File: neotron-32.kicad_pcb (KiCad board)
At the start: 2 copper layers, 166.9 x 140.7 mm, 93 parts, among them J1 Conn_02x06, J10 micro SD Card, J11 Conn_02x13_Top_Bottom, J12 AVR-ISP-6, J13 DE9 Male, J14 DE9 Male, J15 Double-mini-DIN-6, J17 DB15HD_Female, J18 Conn_02x05, J2 Conn_02x06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

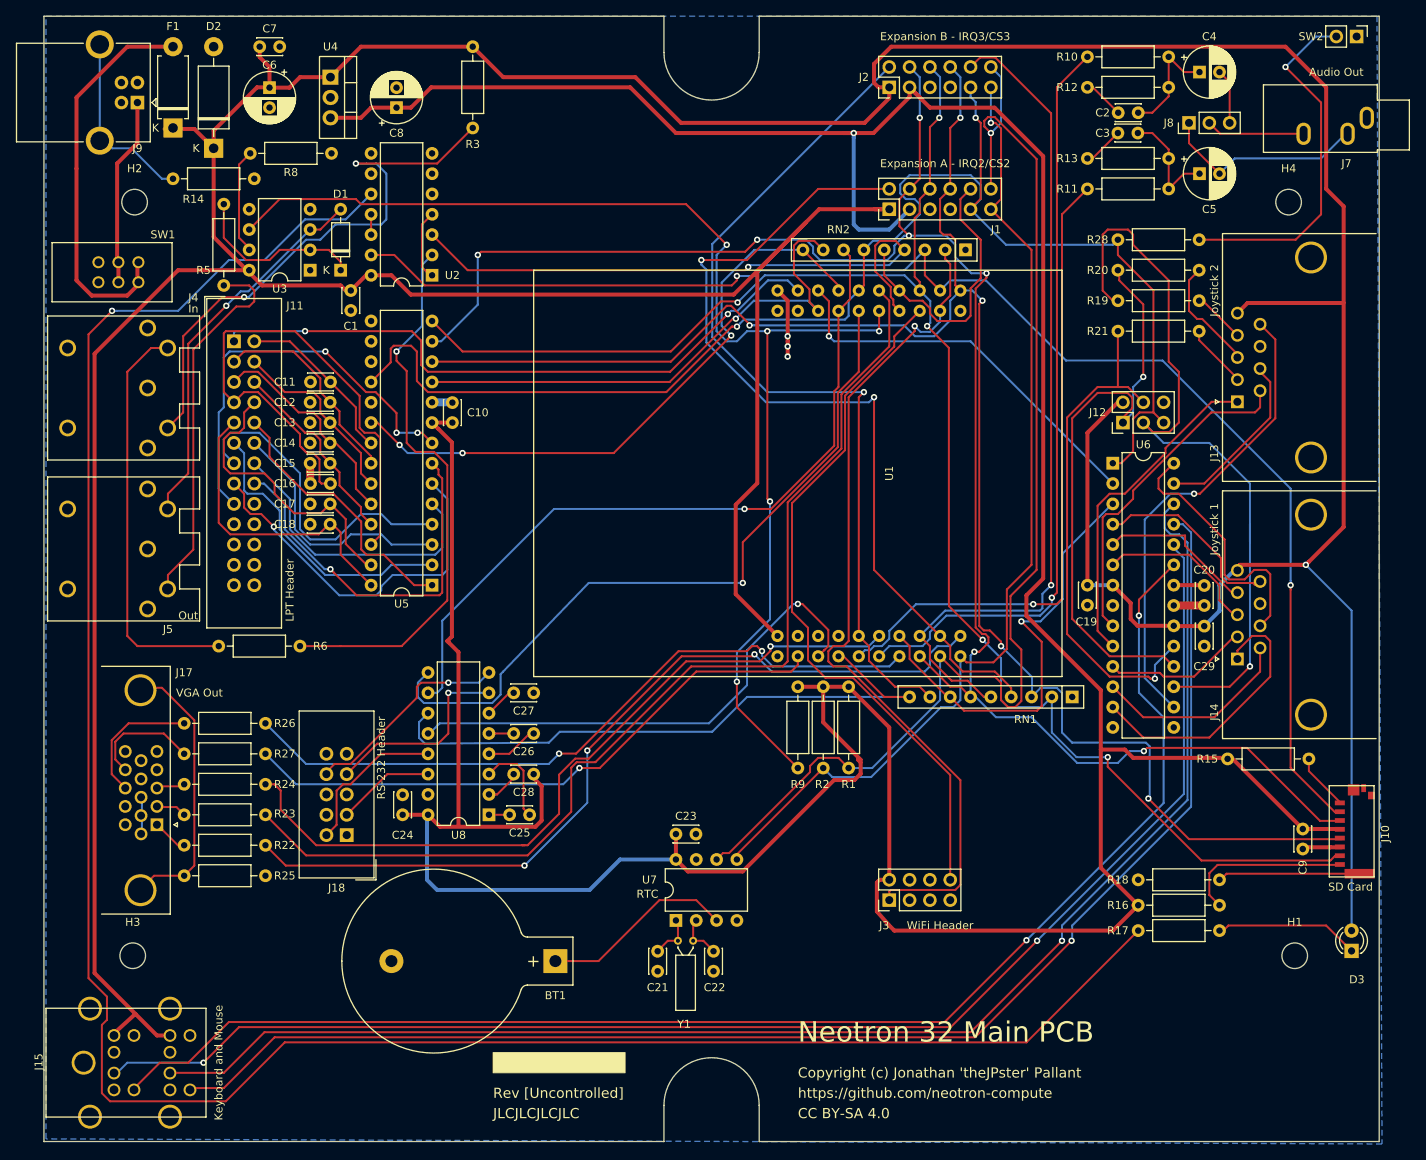
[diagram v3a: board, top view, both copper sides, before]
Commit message: Added Reset switch.
Also added 3D models.
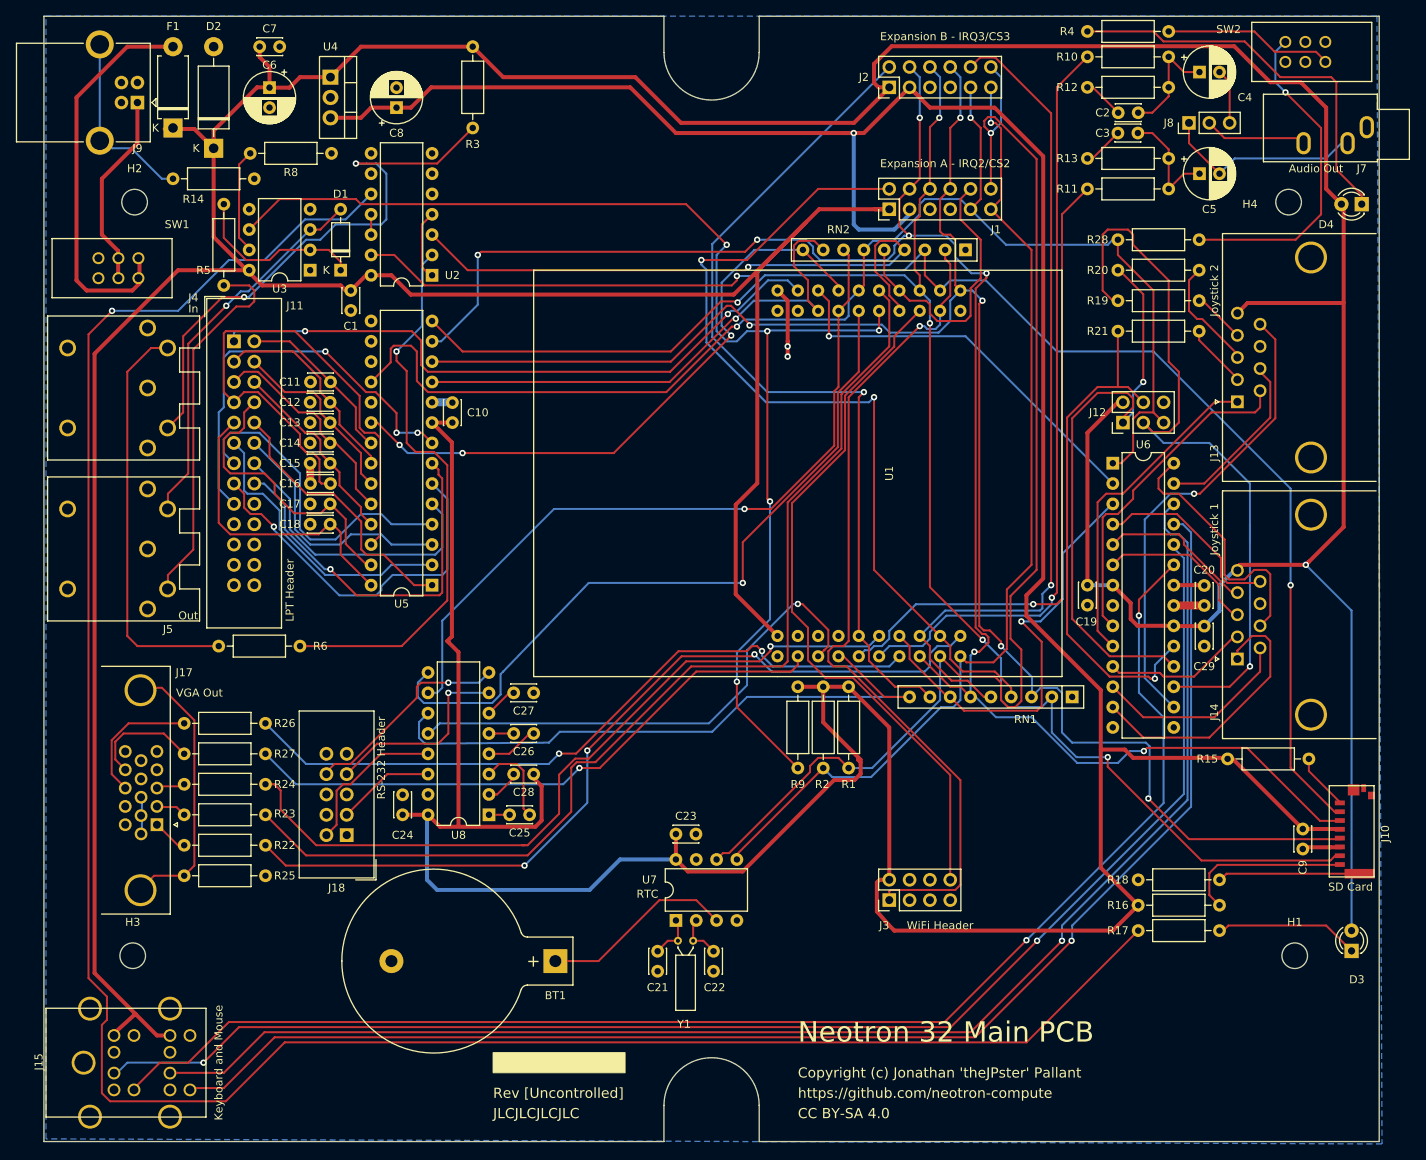
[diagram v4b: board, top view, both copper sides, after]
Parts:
- added D4: Red LED, LED_THT:LED_D3.0mm, F.Cu at (235.6, 41.3)
- added R4: 330, Resistor_THT:R_Axial_DIN0207_L6.3mm_D2.5mm_P10.16mm_Horizontal, F.Cu at (201.3, 19.7)
- SW1: value SW_Push_DPDT -> SW_Push_DPDT_ON_OFF
- SW2: value SW_Push -> SW_Push_DPDT_ON_MO; footprint Connector_PinHeader_2.54mm:PinHeader_1x02_P2.54mm_Vertical -> Neotron 32:PHB2UEETS1A
- moved SW2 5.93 mm to (229.3, 22.2), turned to 180 degrees
- moved J7 1.18 mm to (236.2, 31.7)
- moved SW1 0.51 mm to (79.4, 49.3)
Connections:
- SW2 pad 1: GND -> (no net)
- SW2 pad 2: Net-(R28-Pad2) -> GND
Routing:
- net Net-(D4-Pad1): track 0.00 -> 50.3 mm
- net Net-(R4-Pad2): track 0.00 -> 21.3 mm
- net /~RESET: track 181.3 -> 169.7 mm
- net Net-(R28-Pad2): track 44.7 -> 41.0 mm
- net +5V: track 641.0 -> 638.8 mm
- net Net-(J9-Pad1): track 23.6 -> 25.2 mm
- net /Keyboard, Mouse and Joystick/START_C_JS1: track 23.2 -> 24.0 mm
- net GND: vias 3 -> 2

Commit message: Set version to v1.0.0
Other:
- board text added: "Rev [v1.0.0]"
- board text removed: "Rev [Uncontrolled]"
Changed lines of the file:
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@@
     (title "Neotron 32K Main PCB")
     (date 2019-12-09)
-    (rev [Uncontrolled])
+    (rev [v1.0.0])
     (company github.com/neotron-compute/Neotron-32-Hardware)
     (comment 1 "Copyright (c) Jonathan 'theJPster' Pallant")
@@
     (effects (font (size 1.27 1.27) (thickness 0.15)) (justify left))
   )
-  (gr_text "Rev [Uncontrolled]" (at 127 152.4) (layer F.SilkS)
+  (gr_text "Rev [v1.0.0]" (at 127 152.4) (layer F.SilkS)
     (effects (font (size 1.27 1.27) (thickness 0.15)) (justify left))
   )
